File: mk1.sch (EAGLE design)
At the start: 28 parts, among them U1 IAM-20380, U2 MC34063AD, U3 ADXL345, U4 STM32F407VGT6

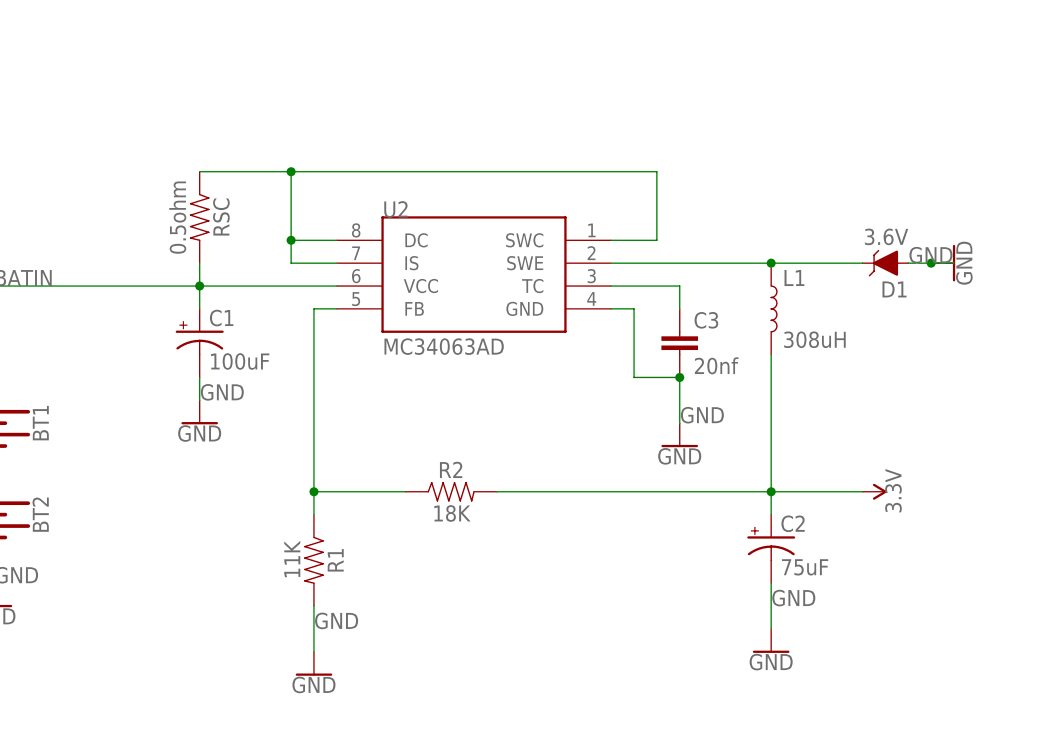
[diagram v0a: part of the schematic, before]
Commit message: Changed values of passive components around mc3406
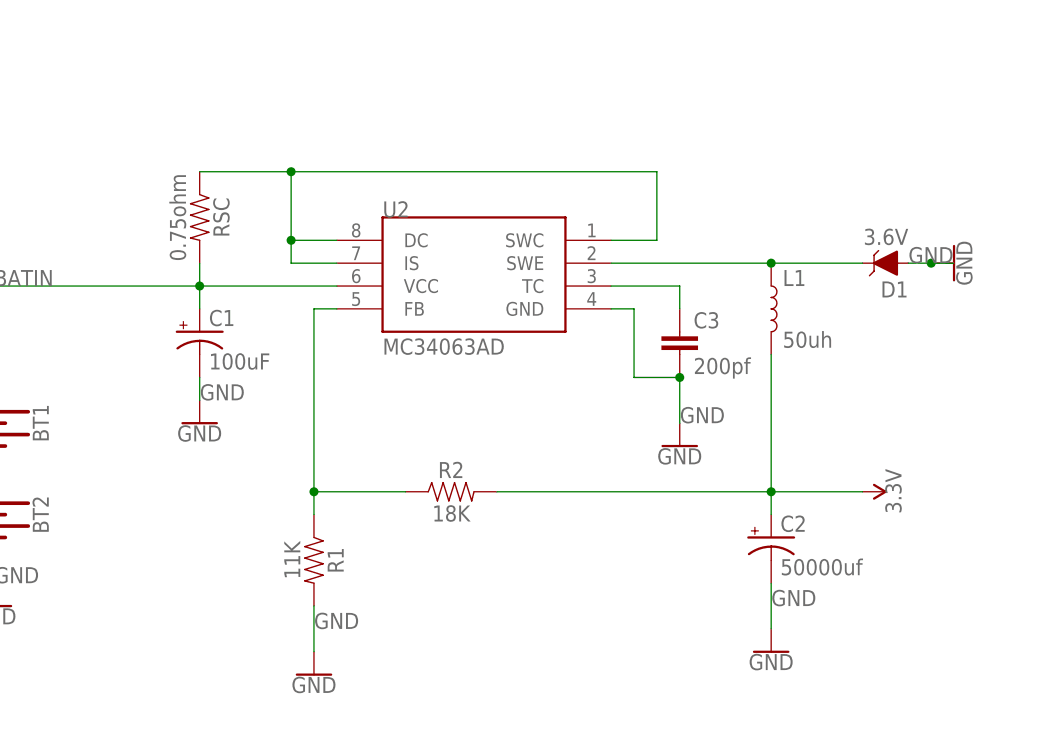
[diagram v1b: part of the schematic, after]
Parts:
- C2: value 75uF -> 50000uf
- C3: value 20nf -> 200pf
- L1: value 308uH -> 50uh
- RSC: value 0.5ohm -> 0.75ohm
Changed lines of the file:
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@@
 <part name="U2" library="mc34063" deviceset="MC34063" device="AD"/>
 <part name="C1" library="SparkFun-Capacitors" deviceset="100UF-POLAR" device="-EIA7343-10V-10%(TANT)" value="100uF"/>
-<part name="RSC" library="SparkFun-Resistors" deviceset="0.3OHM" device="-0805-1/8W-1%" value="0.5ohm"/>
+<part name="RSC" library="SparkFun-Resistors" deviceset="0.3OHM" device="-0805-1/8W-1%" value="0.75ohm"/>
 <part name="R1" library="SparkFun-Resistors" deviceset="0.3OHM" device="-0805-1/8W-1%" value="11K"/>
 <part name="R2" library="SparkFun-Resistors" deviceset="0.3OHM" device="-0805-1/8W-1%" value="18K"/>
-<part name="C2" library="SparkFun-Capacitors" deviceset="100UF-POLAR" device="-EIA7343-10V-10%(TANT)" value="75uF"/>
-<part name="L1" library="SparkFun-Coils" deviceset="INDUCTOR" device="-0805-3.3UH" value="308uH"/>
+<part name="C2" library="SparkFun-Capacitors" deviceset="100UF-POLAR" device="-EIA7343-10V-10%(TANT)" value="50000uf"/>
+<part name="L1" library="SparkFun-Coils" deviceset="INDUCTOR" device="-0805-3.3UH" value="50uh"/>
 <part name="D1" library="SparkFun-DiscreteSemi" deviceset="DIODE-ZENER" device="-BZT52C3V6S" value="3.6V"/>
 <part name="GND1" library="SparkFun-PowerSymbols" deviceset="GND" device=""/>
@@
 <part name="GND5" library="SparkFun-PowerSymbols" deviceset="GND" device=""/>
 <part name="GND9" library="SparkFun-PowerSymbols" deviceset="GND" device=""/>
-<part name="C3" library="SparkFun-Capacitors" deviceset="0.33UF/330NF" device="-0805-50V-10%" value="20nf"/>
+<part name="C3" library="SparkFun-Capacitors" deviceset="0.33UF/330NF" device="-0805-50V-10%" value="200pf"/>
 <part name="C7" library="SparkFun-Capacitors" deviceset="0.33UF/330NF" device="-0805-50V-10%" value="10nf"/>
 <part name="C6" library="SparkFun-Capacitors" deviceset="0.33UF/330NF" device="-0805-50V-10%" value="0.47uf"/>

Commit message: Update Rev 1 with reroute
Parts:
- removed JP1: (no value), adafruit:PINHD-1X3
- added C10: 22uF, SparkFun-Capacitors:22UF-0805-6.3V-20%
- added C9: 0.1uF, SparkFun-Capacitors:0.1UF-0603-25V-5%
- added J1, J2, J3: (no value), Wurth_Elektronik_Electromechanic_Board_to_Board_Connectors_rev18b:61300411121
- added LS1: CSS-0575A-SMT, CSS-0575A-SMT:CSS-0575A-SMT
- added R10, R11: 4.7k, SparkFun-Resistors:4.7KOHM-0603-1/10W-1%
- added R7: 200k, SparkFun-Resistors:200KOHM-0603-1/10W-1%
- added R8: 220k, SparkFun-Resistors:220KOHM-0603-1/10W-1%
- added R9: 43k, SparkFun-Resistors:43KOHM-0603-1/10W-1%
- added U5: LT1529CQTRPBF, LT1529CQTRPBF:LT1529CQTRPBF
- added U6: MPL115A2, MPL115A2:MPL115A2
- added U7: SN65HVD232DR, SN65HVD232DR:SN65HVD232DR
- BT1: SPICEPREFIX (none) -> B
- C1: device SparkFun-Capacitors:100UF-POLAR-EIA7343-10V-10%(TANT) -> SparkFun-Capacitors:100UF-POLAR-1206-6.3V-20%(TANT)
- C2: value 50000uf -> 100uF; device SparkFun-Capacitors:100UF-POLAR-EIA7343-10V-10%(TANT) -> SparkFun-Capacitors:100UF-POLAR-1206-6.3V-20%(TANT)
- C5: value 2.2uf -> 100uF; device SparkFun-Capacitors:100UF-POLAR-EIA7343-10V-10%(TANT) -> SparkFun-Capacitors:100UF-POLAR-1206-6.3V-20%(TANT)
- L1: value 50uh -> 47uh
- U2: SPICEPREFIX (none) -> X
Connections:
- removed net N$15: JP1.2, U4G$1.PA13
- removed net N$16: JP1.1, U4G$1.PA14
- removed net N$6: C7.1, U1.VDDIO, U3.VDD
- new net +3V3: C7.1, U1.VDDIO, U3.VDD, U6.VDD, U7.VCC
- new net BENABLE: U4G$2.PD9, U6.*RST
- new net BSCL: R11.2, U4G$1.PB6, U6.SCL
- new net BSDA: R10.2, U4G$1.PB7, U6.SDA
- new net BSHD: U6.*SHDN
- new net BUZZER: LS1.P, U4G$1.PB2
- new net CANH: J3.2, U7.CANH
- new net CANL: J3.1, U7.CANL
- new net CANRX: U4G$1.PA11, U7.R
- new net CANTX: U4G$1.PA12, U7.D
- new net JTCK: J3.3, U4G$1.PA14
- new net N$18: R7.1, R8.2, U5.SENSE/ADJ
- new net N$19: R8.1, R9.2
- new net N$22: C9.2, U6.CAP
- new net S1IN: J1.2, U4G$2.PC5
- new net S1O: J1.3, U4G$2.PC4
- new net S2IN: J2.2, U4G$1.PB1
- new net S2O: J2.3, U4G$1.PB0
- new net SERVOPWR: U4G$2.PD10, U5.*SHDN
- new net SWDIO: J3.4, U4G$1.PA13
- new net V7+: C10.2, J1.4, J2.4, R7.2, U5.OUTPUT
- net BATIN: now also U5.VIN
- net GND: now also C10.1, C9.1, J1.1, J2.1, LS1.N, R10.1, R11.1, R9.1, U5.GND, U6.GND, U7.GND
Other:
- note added: "18650 Cells"
- note added: "Accelerometer"
- note added: "Barometer"
- note added: "Buck Converter"
- note added: "Buzzer"
- note added: "CAN Transciever"
- note added: "Debug"
- note added: "Gyro"
- note added: "Linear Regulator"
- note added: "Servo Header"
- moved on the sheet: BT1, BT2, LED1, R3

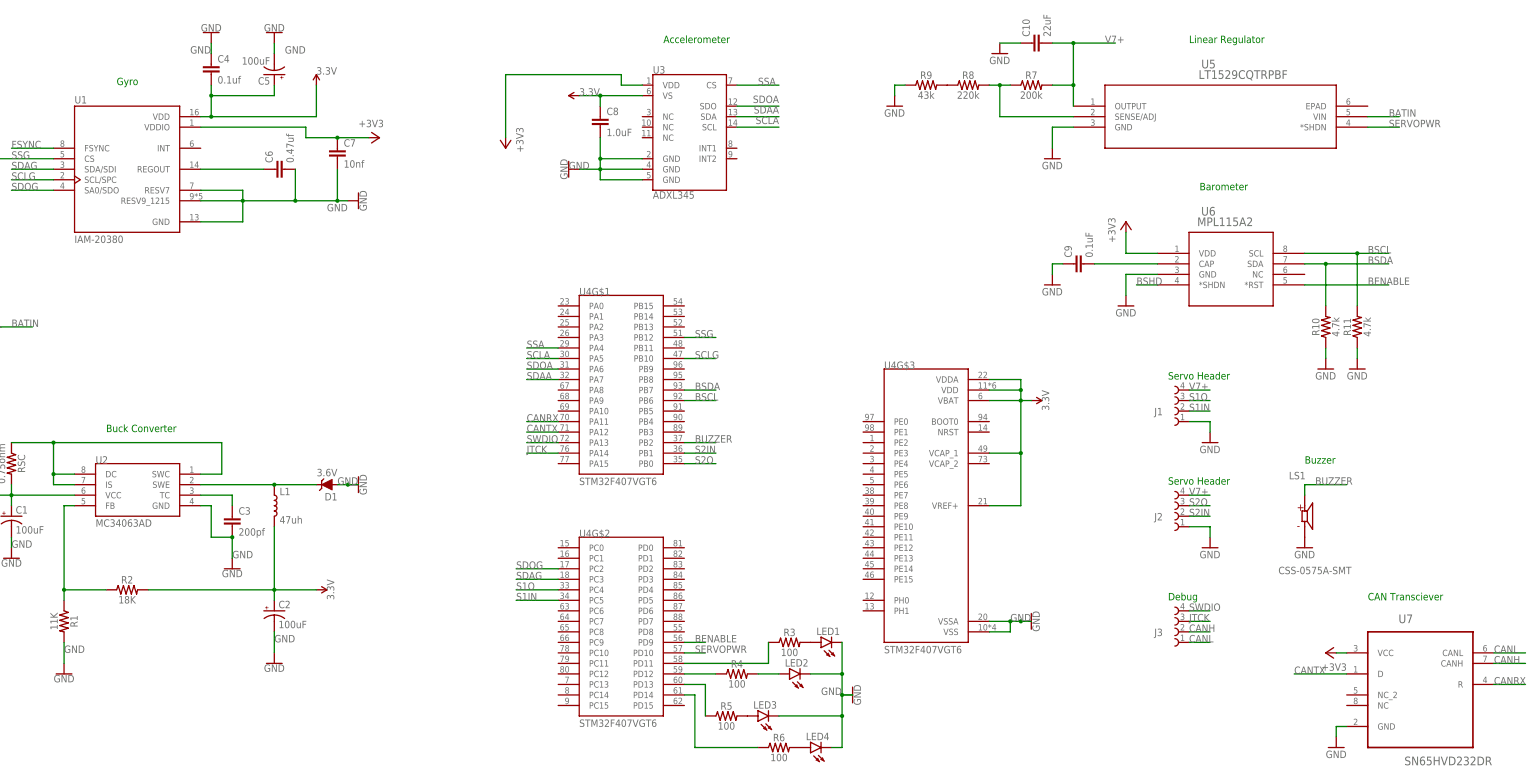
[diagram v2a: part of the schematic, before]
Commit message: Added silkscreen names/logo
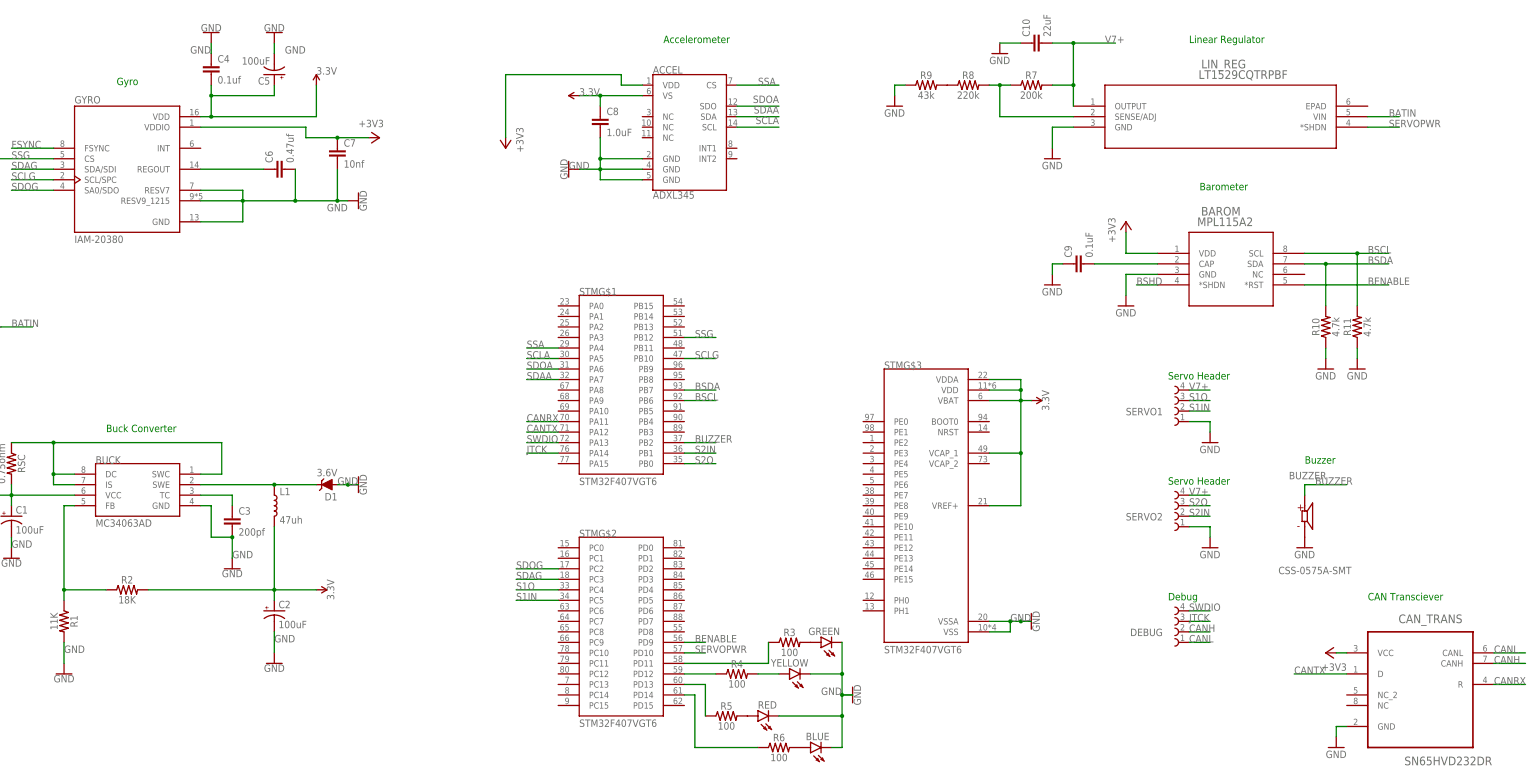
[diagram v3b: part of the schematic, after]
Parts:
- renumbered J1 to SERVO1, J2 to SERVO2, J3 to DEBUG, LED1 to GREEN, LED2 to YELLOW, LED3 to RED, LED4 to BLUE, LS1 to BUZZER, U1 to GYRO, U2 to BUCK, U3 to ACCEL, U4 to STM, U5 to LIN_REG, U6 to BAROM, U7 to CAN_TRANS
